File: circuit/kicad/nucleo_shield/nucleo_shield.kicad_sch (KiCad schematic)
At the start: 8 parts, among them J1 USB_B_Micro, U1 NUCLEO-F401RE, U2 CH340G, Y1 12MHz

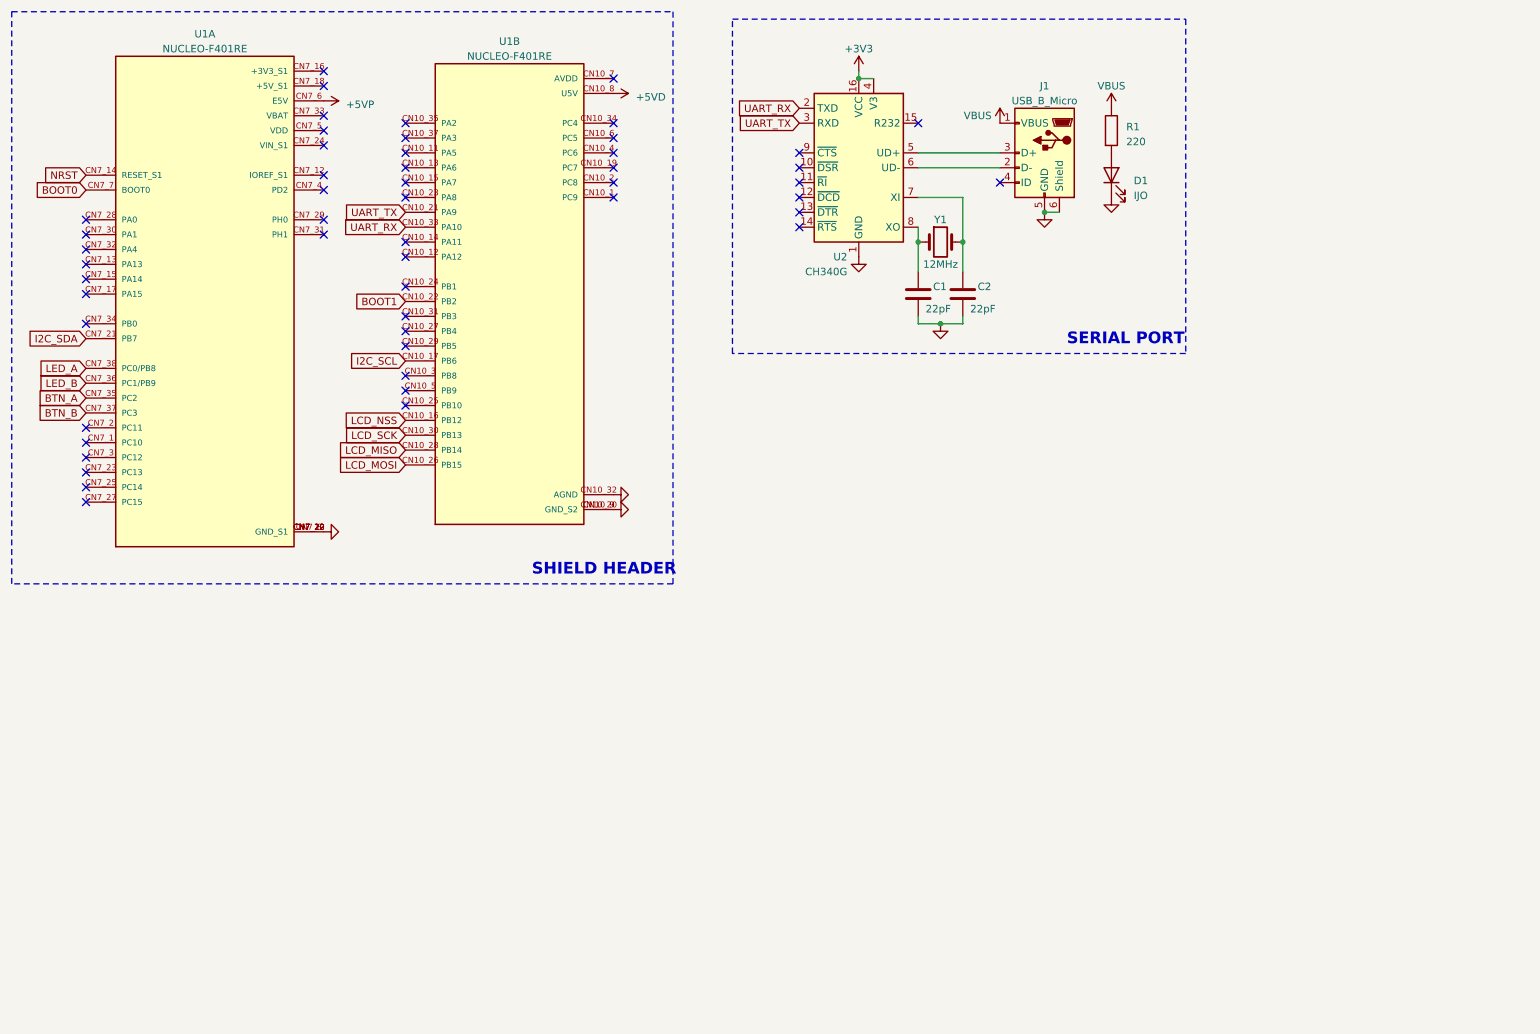
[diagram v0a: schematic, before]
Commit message: Nucleo Shield
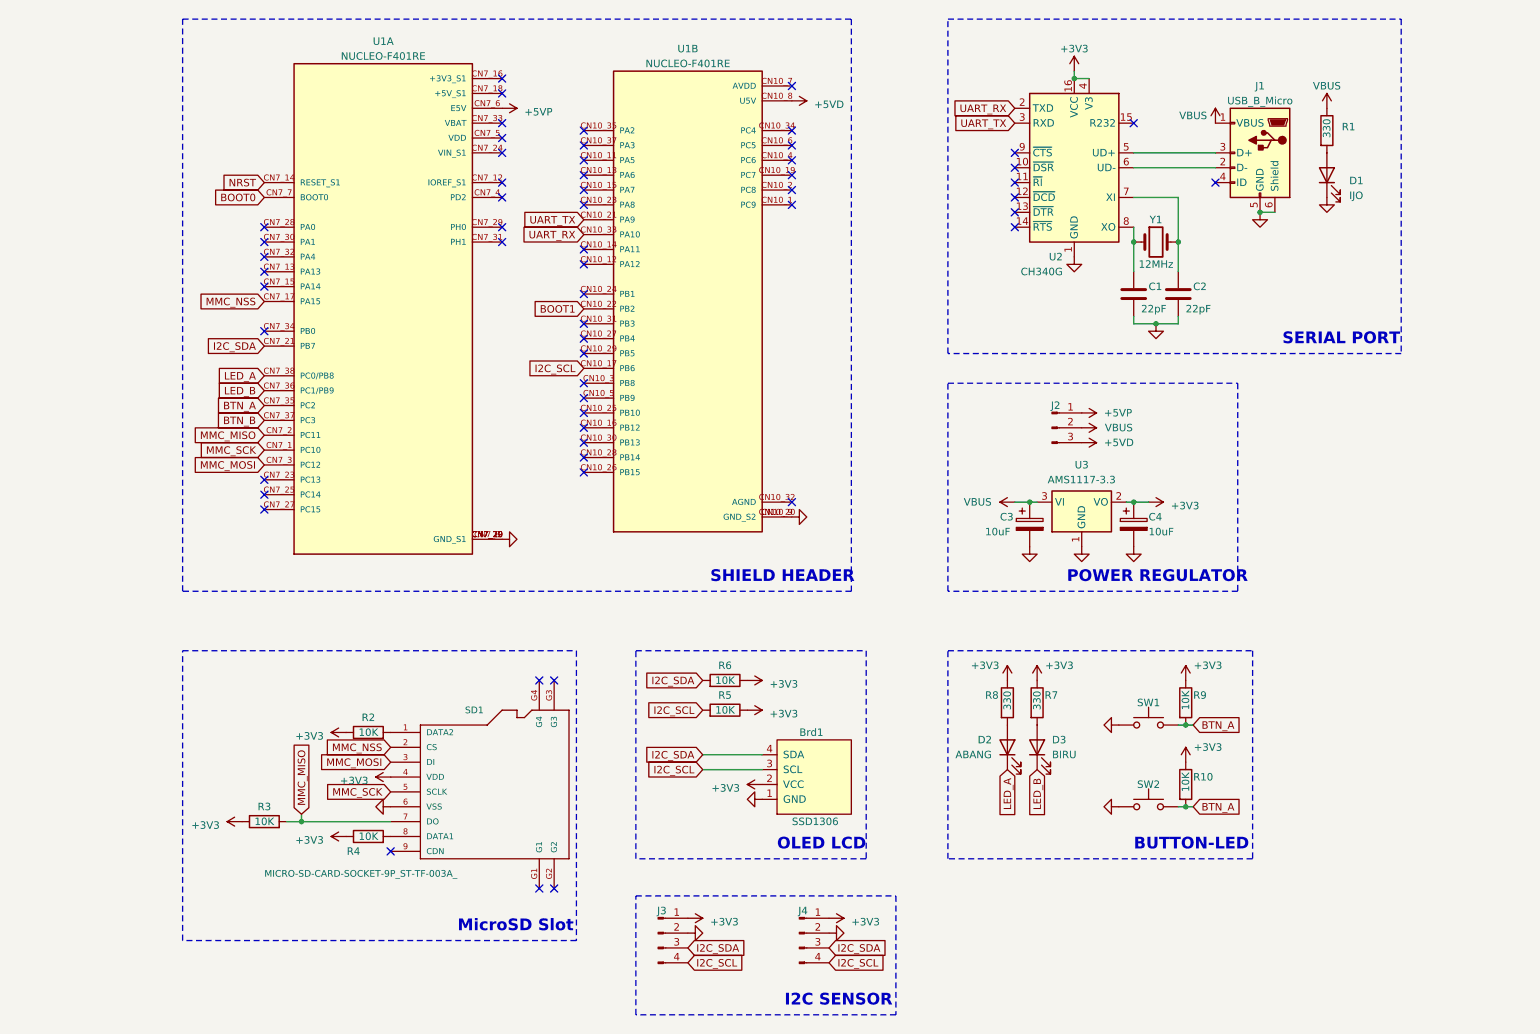
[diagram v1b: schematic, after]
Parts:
- added Brd1: SSD1306, symbol SSD1306-128x64_OLED:SSD1306
- added C3, C4: 10uF, symbol Device:C_Polarized
- added D2: ABANG, symbol Device:LED
- added D3: BIRU, symbol Device:LED
- added J2: Conn_01x03_Pin, symbol Connector:Conn_01x03_Pin
- added J3, J4: Conn_01x04_Pin, symbol Connector:Conn_01x04_Pin
- added R10, R2, R3, R4, R5, R6, R9: 10K, symbol Device:R
- added R7, R8: 330, symbol Device:R
- added SD1: MICRO-SD-CARD-SOCKET-9P_ST-TF-003A_, symbol OPL_Connector:MICRO-SD-CARD-SOCKET-9P_ST-TF-003A_
- added SW1, SW2: SW_Push, symbol Switch:SW_Push
- added U3: AMS1117-3.3, Package_TO_SOT_SMD:SOT-223-3_TabPin2, symbol Regulator_Linear:AMS1117-3.3
- R1: value 220 -> 330
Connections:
- net +3V3: now also Brd1.2 (VCC), C4.1, J3.1 (Pin_1), J4.1 (Pin_1), R10.1, R2.1, R3.1, R4.1, R5.1, R6.1, R7.1, R8.1, R9.1, SD1.4 (VDD), U3.2 (VO)
- net +5VD: now also J2.3 (Pin_3)
- net +5VP: now also J2.1 (Pin_1)
- net BTN_A: now also R10.2, R9.2, SW1.2, SW2.2
- net GND: now also Brd1.1 (GND), C3.2, C4.2, J3.2 (Pin_2), J4.2 (Pin_2), SD1.6 (VSS), SW1.1, SW2.1, U3.1 (GND); no longer U1.CN10_32 (AGND)
- net I2C_SCL: now also Brd1.3 (SCL), J3.4 (Pin_4), J4.4 (Pin_4), R5.2
- net I2C_SDA: now also Brd1.4 (SDA), J3.3 (Pin_3), J4.3 (Pin_3), R6.2
- net LED_A: now also D2.1 (K)
- net LED_B: now also D3.1 (K)
- net VBUS: now also C3.1, J2.2 (Pin_2), U3.3 (VI)
- net MMC_SCK: now reaches U1.CN7_1 (PC10)
- net MMC_SCK: now also SD1.5 (SCLK)
- net MMC_NSS: now reaches U1.CN7_17 (PA15)
- net MMC_NSS: now also SD1.2 (CS)
- net MMC_MISO: now reaches U1.CN7_2 (PC11)
- net MMC_MISO: now also R3.2, SD1.7 (DO)
- net MMC_MOSI: now reaches U1.CN7_3 (PC12)
- net MMC_MOSI: now also SD1.3 (DI)
- net LCD_MISO: no longer names the net of U1.CN10_28 (PB14)
- net LCD_MOSI: no longer names the net of U1.CN10_26 (PB15)
- net LCD_NSS: no longer names the net of U1.CN10_16 (PB12)
- net LCD_SCK: no longer names the net of U1.CN10_30 (PB13)
- new net: R2.2, SD1.1 (DATA2)
- new net: R4.2, SD1.8 (DATA1)
- new net: D2.2 (A), R8.2
- new net: D3.2 (A), R7.2
- no-connect marks 52 -> 58
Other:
- note added: "BUTTON-LED"
- note added: "I2C SENSOR"
- note added: "MicroSD Slot"
- note added: "OLED LCD"
- note added: "POWER REGULATOR"
- moved on the sheet: C1, C2, D1, J1, R1, U1A, U1B, U2, Y1

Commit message: Nucleo Shield
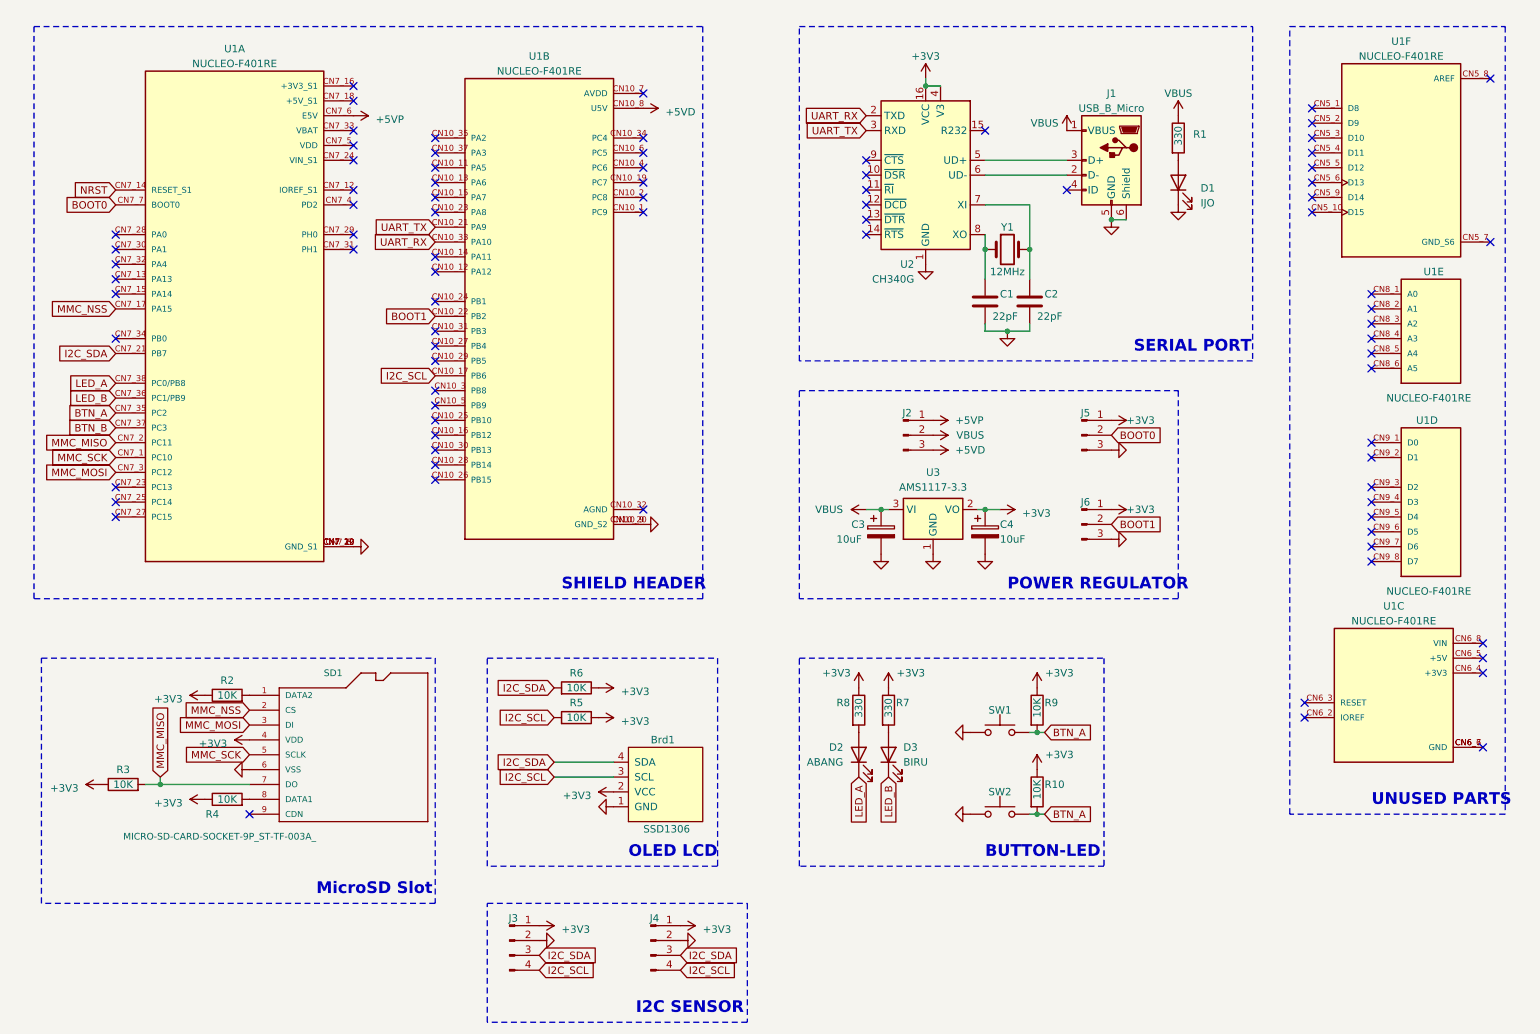
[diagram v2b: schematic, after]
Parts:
- added J5, J6: Conn_01x03_Pin, Connector_PinHeader_2.54mm:PinHeader_1x03_P2.54mm_Vertical, symbol Connector:Conn_01x03_Pin
- added unit 5 of U1
- added unit 3 of U1
- added unit 6 of U1
- added unit 4 of U1
- Brd1: footprint (none) -> SSD1306:128x64OLED
- C1, C2: footprint (none) -> Capacitor_SMD:C_1206_3216Metric_Pad1.33x1.80mm_HandSolder
- C3, C4: footprint (none) -> Capacitor_SMD:CP_Elec_4x5.3
- D1, D2, D3: footprint (none) -> LED_SMD:LED_1206_3216Metric_Pad1.42x1.75mm_HandSolder
- J1: footprint (none) -> Connector_USB:USB_Micro-B_Wuerth_629105150521
- J2: footprint (none) -> Connector_PinHeader_2.54mm:PinHeader_1x03_P2.54mm_Vertical
- J3, J4: footprint (none) -> Connector_PinHeader_2.54mm:PinHeader_1x04_P2.54mm_Vertical
- R1, R10, R2, R3, R4, R5, R6, R7, R8, R9: footprint (none) -> Resistor_SMD:R_1206_3216Metric_Pad1.30x1.75mm_HandSolder
- SD1: footprint (none) -> OPL_Connector:MICRO-SD9+4P-SMD-16.1X14.5X1.85MM
- SW1, SW2: footprint (none) -> Button_Switch_THT:SW_PUSH_6mm
- U1: footprint ST_NUCLEO-F401RE -> NUCLEO-F401RE:ST_NUCLEO-F401RE
- Y1: footprint (none) -> Crystal:Crystal_HC49-U_Vertical
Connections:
- net +3V3: now also J5.1 (Pin_1), J6.1 (Pin_1)
- net BOOT0: now also J5.2 (Pin_2)
- net BOOT1: now also J6.2 (Pin_2)
- net GND: now also J5.3 (Pin_3), J6.3 (Pin_3)
- new net: U1.CN6_6 (GND), U1.CN6_7 (GND)
- no-connect marks 58 -> 84
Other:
- note added: "UNUSED PARTS"
- moved on the sheet: Brd1, C1, C2, C3, C4, D1, D2, D3, J1, J2, J3, J4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

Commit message: Nucleo Shield
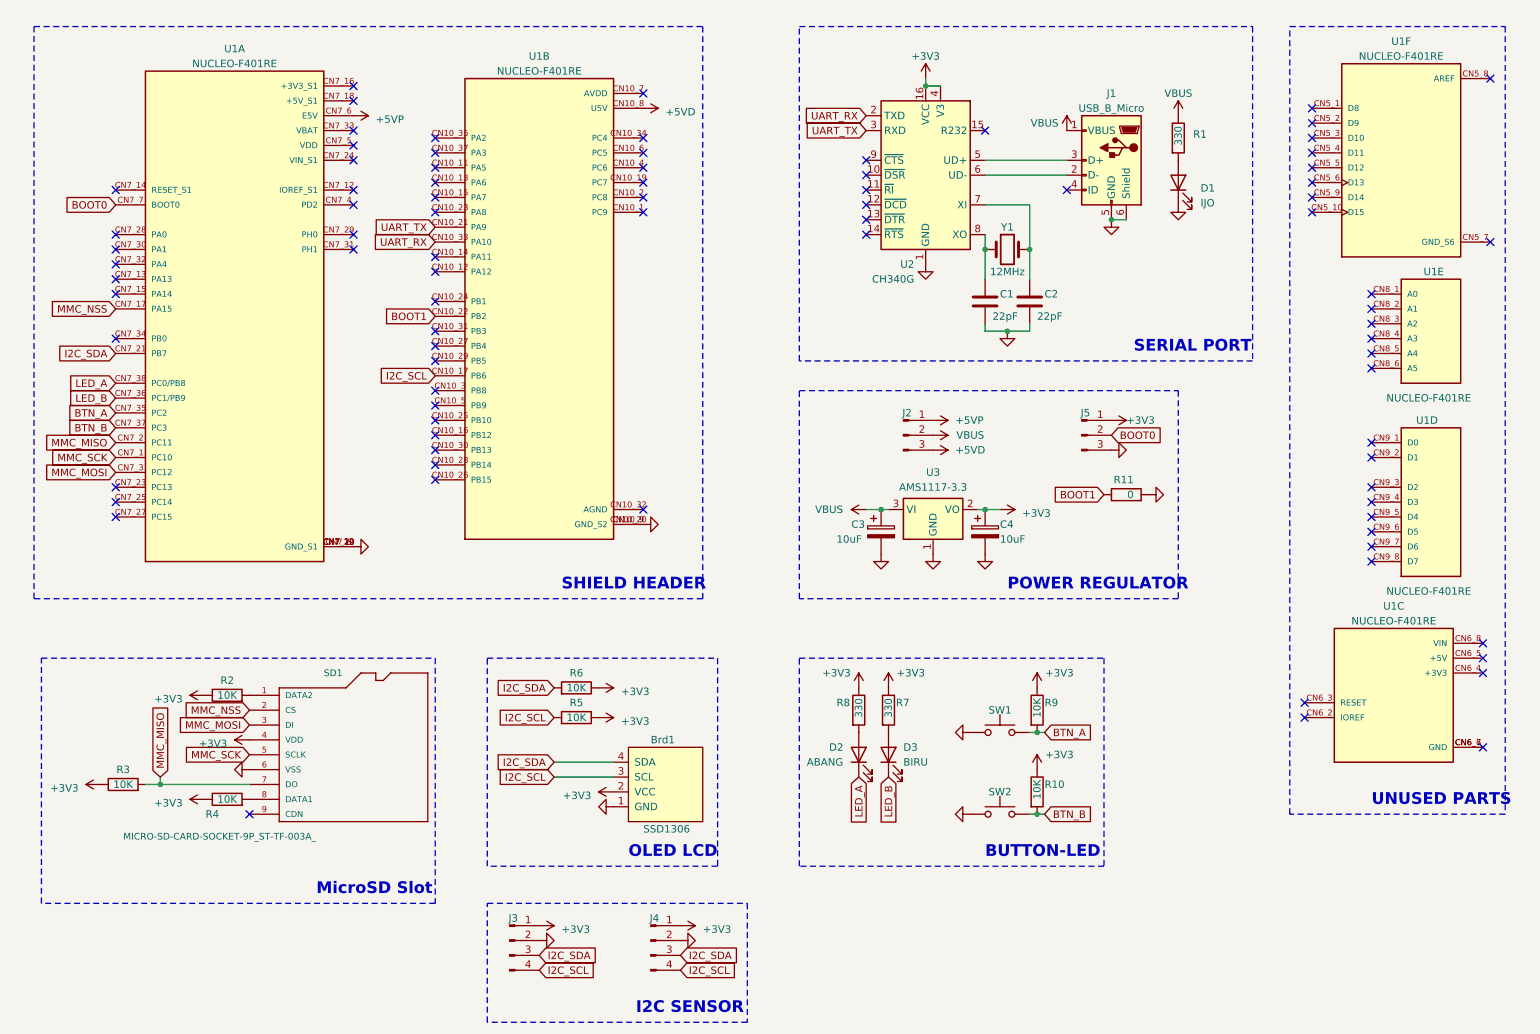
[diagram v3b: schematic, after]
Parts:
- removed J6: Conn_01x03_Pin, Connector_PinHeader_2.54mm:PinHeader_1x03_P2.54mm_Vertical, symbol Connector:Conn_01x03_Pin
- added R11: 0, Resistor_SMD:R_0805_2012Metric_Pad1.20x1.40mm_HandSolder, symbol Device:R
- C1, C2: footprint Capacitor_SMD:C_1206_3216Metric_Pad1.33x1.80mm_HandSolder -> Capacitor_SMD:C_0805_2012Metric_Pad1.18x1.45mm_HandSolder
- D1, D2, D3: footprint LED_SMD:LED_1206_3216Metric_Pad1.42x1.75mm_HandSolder -> LED_SMD:LED_0805_2012Metric_Pad1.15x1.40mm_HandSolder
- R1, R10, R2, R3, R4, R5, R6, R7, R8, R9: footprint Resistor_SMD:R_1206_3216Metric_Pad1.30x1.75mm_HandSolder -> Resistor_SMD:R_0805_2012Metric_Pad1.20x1.40mm_HandSolder
- Y1: footprint Crystal:Crystal_HC49-U_Vertical -> Crystal:Crystal_HC49-4H_Vertical
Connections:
- net BOOT1: now also R11.1
- net BTN_A: no longer R10.2, SW2.2
- net BTN_B: now also R10.2, SW2.2
- net GND: now also R11.2
- net NRST: no longer names the net of U1.CN7_14 (RESET_S1)
- no-connect marks 84 -> 85
